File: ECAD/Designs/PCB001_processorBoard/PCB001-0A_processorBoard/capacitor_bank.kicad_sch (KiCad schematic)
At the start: 14 parts

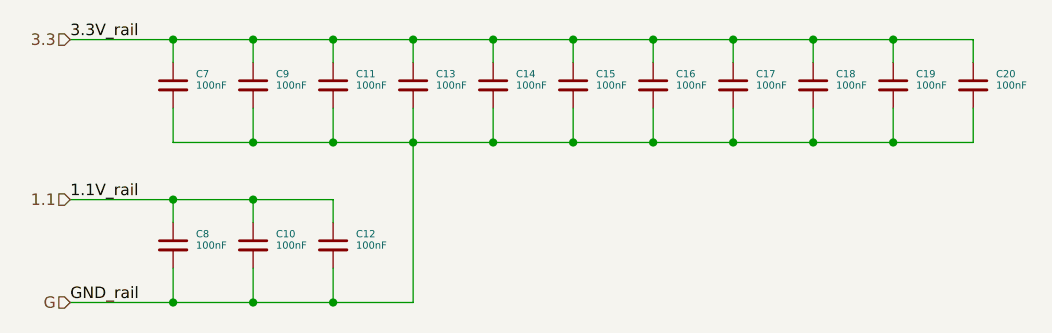
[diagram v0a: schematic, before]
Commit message: updated schematics
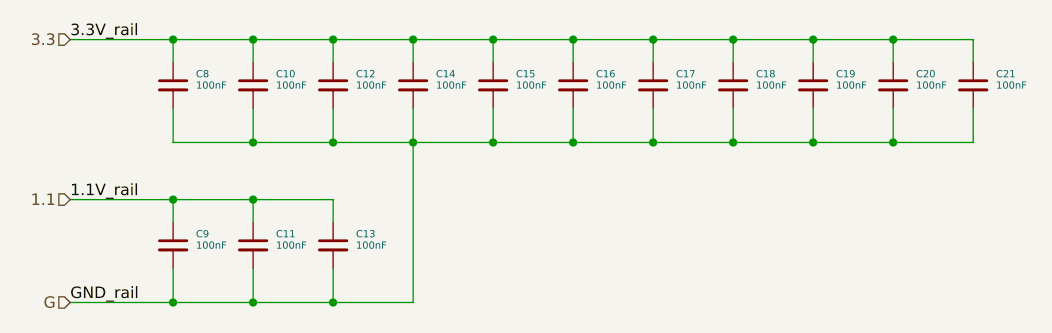
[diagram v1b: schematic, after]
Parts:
- renumbered C9 to C10, C10 to C11, C11 to C12, C12 to C13, C13 to C14, C14 to C15, C15 to C16, C16 to C17, C17 to C18, C18 to C19, C19 to C20, C20 to C21, C7 to C8, C8 to C9
